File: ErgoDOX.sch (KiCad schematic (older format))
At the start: 63 parts, among them J1 USB, J2 3.5mm, J3 JMP, J4 JMP, SW0:10 SW0:3, SW0:11 SW0:2, SW0:12 SW0:1, SW0:7 SW0:6, SW0:8 SW0:5, SW0:9 SW0:4, SW1:10 SW1:3, SW1:11 SW1:2, SW1:12 SW1:1, SW1:13 SW1:0, SW1:9 SW1:4, SW2:10 SW2:3, SW2:11 SW2:2, SW2:12 SW2:1, SW2:13 SW2:0, SW2:7 SW2:6, SW2:8 SW2:5, SW2:9 SW2:4, SW3:10 SW3:3, SW3:11 SW3:2, SW3:12 SW3:1, SW3:13 SW3:0, SW3:8 SW3:5, SW3:9 SW3:4, SW4:10 SW4:3, SW4:11 SW4:2, SW4:12 SW4:1, SW4:13 SW4:0, SW4:7 SW4:6, SW4:8 SW4:5, SW4:9 SW4:4, SW5:10 SW5:3, SW5:11 SW5:2, SW5:12 SW5:1, SW5:13 SW5:0, SW5:7 SW5:6, SW5:8 SW5:5, SW5:9 SW5:4, U1 ProMicro, U2 MCP23018

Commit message: Change IO Expander to MCP23017. Add a logo
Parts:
- removed JP1, JP2: JUMPER, symbol JUMPER
- removed U2: MCP23018, symbol MCP23018
- added U2: MCP23017, symbol MCP23017
- SW0:10, SW0:11, SW0:12, SW0:7, SW0:8, SW0:9, SW1:10, SW1:11, SW1:12, SW1:13, SW1:9, SW2:10, SW2:11, SW2:12, SW2:13, SW2:7, SW2:8, SW2:9, SW3:10, SW3:11, SW3:12, SW3:13, SW3:8, SW3:9, SW4:10, SW4:11, SW4:12, SW4:13, SW4:7, SW4:8, SW4:9, SW5:10, SW5:11, SW5:12, SW5:13, SW5:7, SW5:8, SW5:9: symbol SWITCH_DIODE -> SWITCH_DIODE-RESCUE-ErgoDOX
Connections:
- no-connect marks 12 -> 9

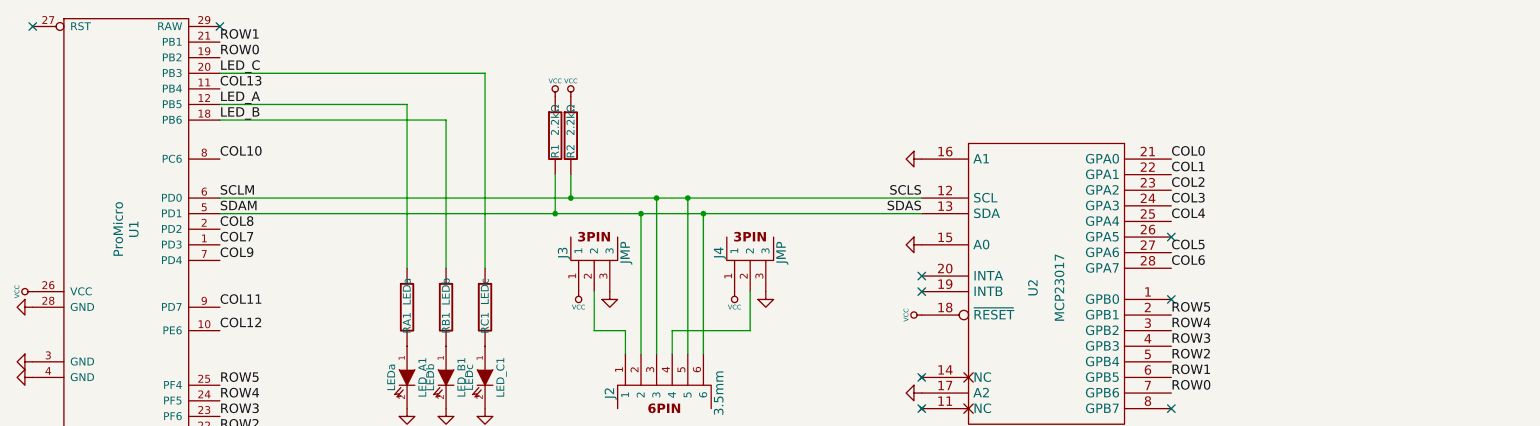
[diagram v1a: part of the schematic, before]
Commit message: Change Micro Pro to left hand
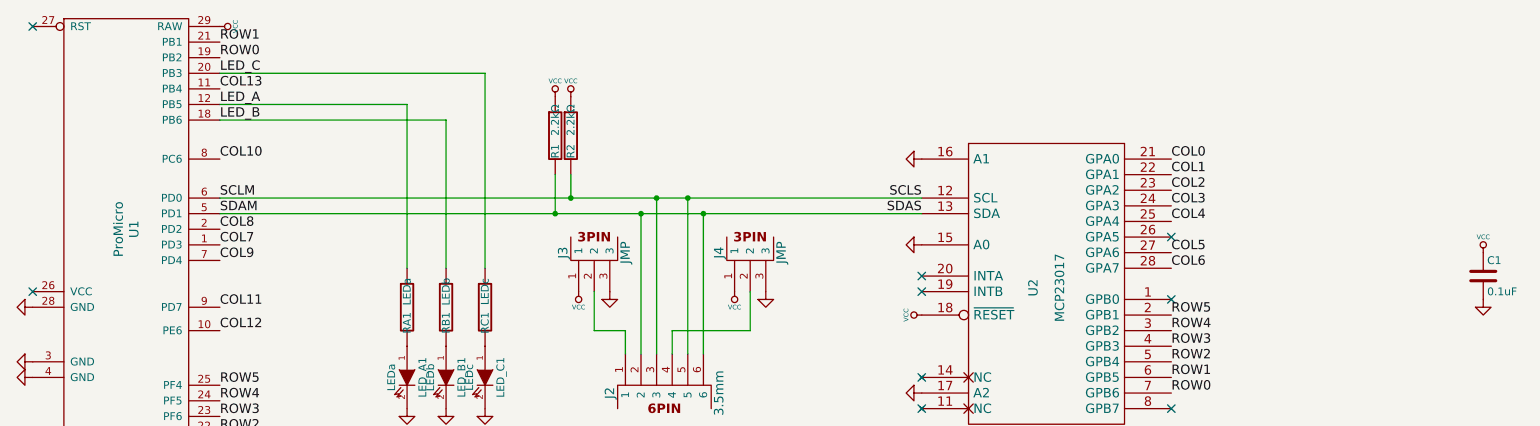
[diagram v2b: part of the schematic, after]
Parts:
- added C1: 0.1uF, symbol C
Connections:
- net GND: now also C1.2
- net VCC: now also U1.29 (RAW), C1.1; no longer U1.26 (VCC)
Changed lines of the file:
@@
 LIBS:ErgoDOX-rescue
 LIBS:component
+LIBS:74xgxx
+LIBS:74xx
+LIBS:ac-dc
+LIBS:actel
+LIBS:adc-dac
+LIBS:Altera
+LIBS:analog_devices
+LIBS:analog_switches
+LIBS:atmel
+LIBS:audio
+LIBS:brooktre
+LIBS:cmos_ieee
+LIBS:cmos4000
+LIBS:conn
+LIBS:contrib
+LIBS:cypress
+LIBS:dc-dc
+LIBS:device
+LIBS:digital-audio
+LIBS:diode
+LIBS:display
+LIBS:dsp
+LIBS:elec-unifil
+LIBS:ESD_Protection
+LIBS:ftdi
+LIBS:gennum
+LIBS:graphic
+LIBS:hc11
+LIBS:intel
+LIBS:interface
+LIBS:ir
+LIBS:Lattice
+LIBS:linear
+LIBS:logo
+LIBS:maxim
+LIBS:memory
+LIBS:microchip
+LIBS:microchip_dspic33dsc
+LIBS:microchip_pic10mcu
+LIBS:microchip_pic12mcu
+LIBS:microchip_pic16mcu
+LIBS:microchip_pic18mcu
+LIBS:microchip_pic32mcu
+LIBS:microcontrollers
+LIBS:motor_drivers
+LIBS:motorola
+LIBS:msp430
+LIBS:nordicsemi
+LIBS:nxp_armmcu
+LIBS:onsemi
+LIBS:opto
+LIBS:Oscillators
+LIBS:philips
+LIBS:power
+LIBS:Power_Management
+LIBS:powerint
+LIBS:pspice
+LIBS:references
+LIBS:regul
+LIBS:relays
+LIBS:rfcom
+LIBS:sensors
+LIBS:silabs
+LIBS:siliconi
+LIBS:stm8
+LIBS:stm32
+LIBS:supertex
+LIBS:switches
+LIBS:texas
+LIBS:transf
+LIBS:transistors
+LIBS:ttl_ieee
+LIBS:valves
+LIBS:video
+LIBS:Xicor
+LIBS:xilinx
+LIBS:Zilog
 LIBS:ErgoDOX-cache
 EELAYER 25 0
@@
 $EndComp
 $Comp
-L VCC #PWR013
+L VCC #PWR012
 U 1 1 4FFF4300
 P 4550 4150
-F 0 "#PWR013" H 4550 4250 30  0001 C CNN
+F 0 "#PWR012" H 4550 4250 30  0001 C CNN
 F 1 "VCC" H 4550 4250 30  0000 C CNN
 F 2 "" H 4550 4150 60  0001 C CNN
@@
 $EndComp
 $Comp
-L GND #PWR014
+L GND #PWR013
 U 1 1 4FFF43E7
 P 4950 4100
-F 0 "#PWR014" H 4950 4100 30  0001 C CNN
+F 0 "#PWR013" H 4950 4100 30  0001 C CNN
 F 1 "GND" H 4950 4030 30  0001 C CNN
 F 2 "" H 4950 4100 60  0001 C CNN
@@
 NoConn ~ 6450 3750
 $Comp
-L GND #PWR015
+L GND #PWR014
 U 1 1 50028213
 P 700 3550
-F 0 "#PWR015" H 700 3550 30  0001 C CNN
+F 0 "#PWR014" H 700 3550 30  0001 C CNN
 F 1 "GND" H 700 3480 30  0001 C CNN
 F 2 "" H 700 3550 60  0001 C CNN
@@
 COL9
 $Comp
-L VCC #PWR017
+L VCC #PWR015
 U 1 1 500D1293
-P 750 3000
-F 0 "#PWR017" H 750 3100 30  0001 C CNN
-F 1 "VCC" H 750 3100 30  0000 C CNN
-F 2 "" H 750 3000 60  0001 C CNN
-F 3 "" H 750 3000 60  0001 C CNN
-	1    750  3000
-	0    -1   -1   0
+P 1950 1300
+F 0 "#PWR015" H 1950 1400 30  0001 C CNN
+F 1 "VCC" H 1950 1400 30  0000 C CNN
+F 2 "" H 1950 1300 60  0001 C CNN
+F 3 "" H 1950 1300 60  0001 C CNN
+	1    1950 1300
+	0    1    1    0
 $EndComp
 $Comp
@@
 F 3 "" H 7450 4750 60  0001 C CNN
 	1    7450 4750
-	1    0    0    -1
-$EndComp
-$Comp
-L ProMicro U1
-U 1 1 5760DCFA
-P 1350 2600
-F 0 "U1" V 1400 2600 60  0000 C CNN
-F 1 "ProMicro" V 1300 2600 60  0000 C CNN
-F 2 "" H 1350 2600 60  0000 C CNN
-F 3 "" H 1350 2600 60  0000 C CNN
-	1    1350 2600
 	1    0    0    -1
 $EndComp
@@
 Wire Wire Line
 	3650 1600 1950 1600
-NoConn ~ 1950 1300
-$Comp
-L GND #PWR019
+$Comp
+L GND #PWR016
 U 1 1 576F2DDE
 P 700 3100
-F 0 "#PWR019" H 700 3100 30  0001 C CNN
+F 0 "#PWR016" H 700 3100 30  0001 C CNN
 F 1 "GND" H 700 3030 30  0001 C CNN
 F 2 "" H 700 3100 60  0000 C CNN
@@
 $EndComp
 $Comp
-L GND #PWR020
+L GND #PWR017
 U 1 1 57617086
 P 6400 2150
-F 0 "#PWR020" H 6400 2150 30  0001 C CNN
+F 0 "#PWR017" H 6400 2150 30  0001 C CNN
 F 1 "GND" H 6400 2080 30  0001 C CNN
 F 2 "" H 6400 2150 60  0001 C CNN
@@
 $EndComp
 $Comp
-L GND #PWR021
+L GND #PWR018
 U 1 1 5761A8AF
 P 6400 3650
-F 0 "#PWR021" H 6400 3650 30  0001 C CNN
+F 0 "#PWR018" H 6400 3650 30  0001 C CNN
 F 1 "GND" H 6400 3580 30  0001 C CNN
 F 2 "" H 6400 3650 60  0001 C CNN
@@
 $EndComp
 $Comp
-L VCC #PWR022
+L VCC #PWR019
 U 1 1 5761B3CF
 P 6450 3150
-F 0 "#PWR022" H 6450 3250 30  0001 C CNN
+F 0 "#PWR019" H 6450 3250 30  0001 C CNN
 F 1 "VCC" H 6450 3250 30  0000 C CNN
 F 2 "" H 6450 3150 60  0000 C CNN
@@
 $EndComp
 NoConn ~ 8050 2650
+$Comp
+L ProMicro U1
+U 1 1 5760DCFA
+P 1350 2600
+F 0 "U1" V 1400 2600 60  0000 C CNN
+F 1 "ProMicro" V 1300 2600 60  0000 C CNN
+F 2 "" H 1350 2600 60  0000 C CNN
+F 3 "" H 1350 2600 60  0000 C CNN
+	1    1350 2600
+	1    0    0    -1
+$EndComp
+NoConn ~ 750  3000
+$Comp
+L C C1
+U 1 1 57825DD2
+P 10050 2900
+F 0 "C1" H 10075 3000 50  0000 L CNN
+F 1 "0.1uF" H 10075 2800 50  0000 L CNN
+F 2 "" H 10088 2750 50  0000 C CNN
+F 3 "" H 10050 2900 50  0000 C CNN
+	1    10050 2900
+	1    0    0    -1
+$EndComp
+$Comp
+L VCC #PWR?
+U 1 1 578269AB
+P 10050 2750
+F 0 "#PWR?" H 10050 2850 30  0001 C CNN
+F 1 "VCC" H 10050 2850 30  0000 C CNN
+F 2 "" H 10050 2750 60  0000 C CNN
+F 3 "" H 10050 2750 60  0000 C CNN
+	1    10050 2750
+	1    0    0    -1
+$EndComp
+$Comp
+L GND #PWR?
+U 1 1 57827429
+P 10050 3100
+F 0 "#PWR?" H 10050 3100 30  0001 C CNN
+F 1 "GND" H 10050 3030 30  0001 C CNN
+F 2 "" H 10050 3100 60  0000 C CNN
+F 3 "" H 10050 3100 60  0000 C CNN
+	1    10050 3100
+	1    0    0    -1
+$EndComp
 $EndSCHEMATC

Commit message: add 0.1uF capacitor
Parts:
- C1: footprint (none) -> Capacitors_ThroughHole:C_Rect_L7_W2_P5
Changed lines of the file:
@@
 F 0 "C1" H 10075 3000 50  0000 L CNN
 F 1 "0.1uF" H 10075 2800 50  0000 L CNN
-F 2 "" H 10088 2750 50  0000 C CNN
+F 2 "Capacitors_ThroughHole:C_Rect_L7_W2_P5" H 10088 2750 50  0001 C CNN
 F 3 "" H 10050 2900 50  0000 C CNN
 	1    10050 2900
